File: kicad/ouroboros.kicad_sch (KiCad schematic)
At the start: 121 parts, among them J1 Eurorack Mono Jack, J10 Conn_01x03_Male, J11 Eurorack Mono Jack, J12 Eurorack Mono Jack, J13 Eurorack Mono Jack, J14 Eurorack Mono Jack, J19 Eurorack Mono Jack, J2 Eurorack Mono Jack, J20 Eurorack Mono Jack, J21 Eurorack Mono Jack, J22 Eurorack Mono Jack, J23 Eurorack Mono Jack, J24 Eurorack Mono Jack, J25 Eurorack Mono Jack, J26 Eurorack Mono Jack, J27 Eurorack Mono Jack, J28 Conn_01x06_Male, J29 Conn_01x04_Male, J3 Eurorack Mono Jack, J30 Conn_01x04_Male, J31 Conn_01x04_Male, J32 Conn_01x06_Male, J33 Conn_01x04_Male, J34 Conn_01x08_Male, J35 Conn_01x08_Male, J36 Eurorack Power Small, J38 Conn_02x04_Odd_Even, J4 Eurorack Mono Jack, J40 Conn_01x08_Female, J41 Conn_01x08_Female, J42 Conn_01x04_Female, J43 Conn_01x06_Female, J44 Conn_01x04_Female, J45 Conn_01x04_Female, J46 Conn_01x04_Female, J47 Conn_01x06_Female, J5 Eurorack Mono Jack, J6 Eurorack Mono Jack, J7 Eurorack Mono Jack, J8 Eurorack Mono Jack, J9 Eurorack Mono Jack, U1 TL074, U8 L78L05_TO92

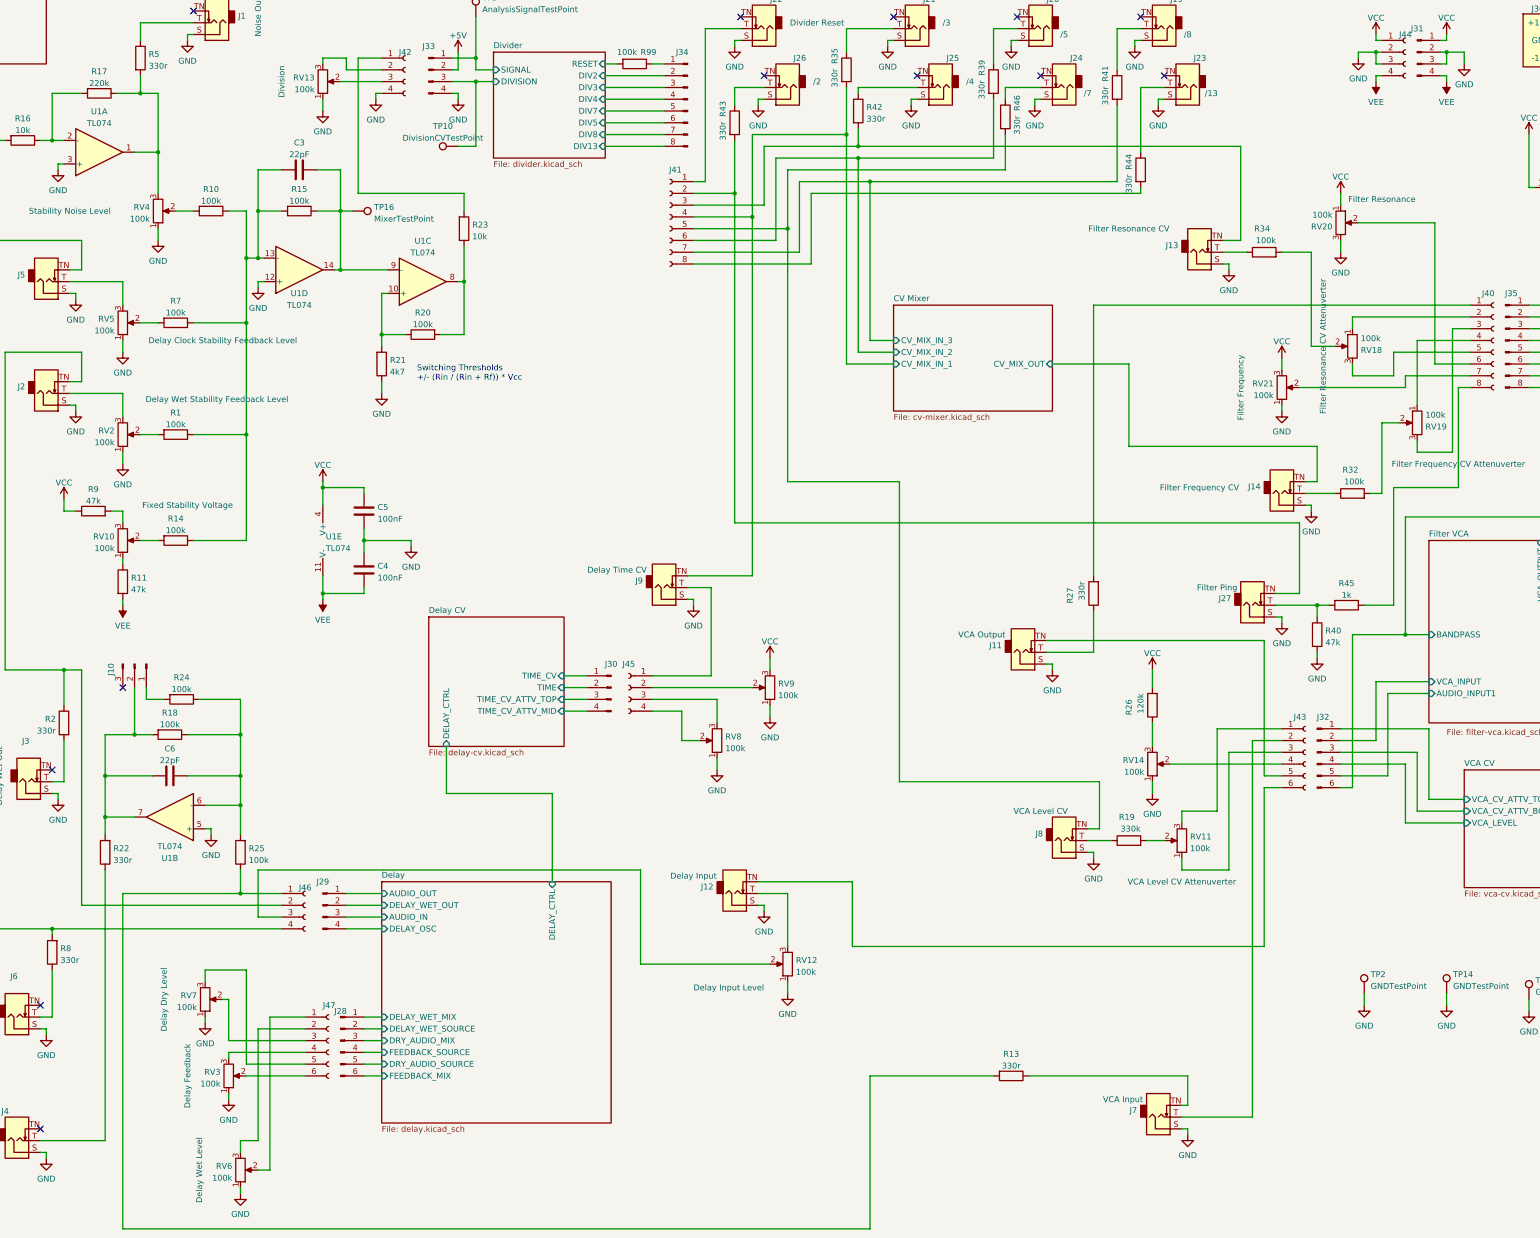
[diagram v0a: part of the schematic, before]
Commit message: Updating bom and creating part numbers list
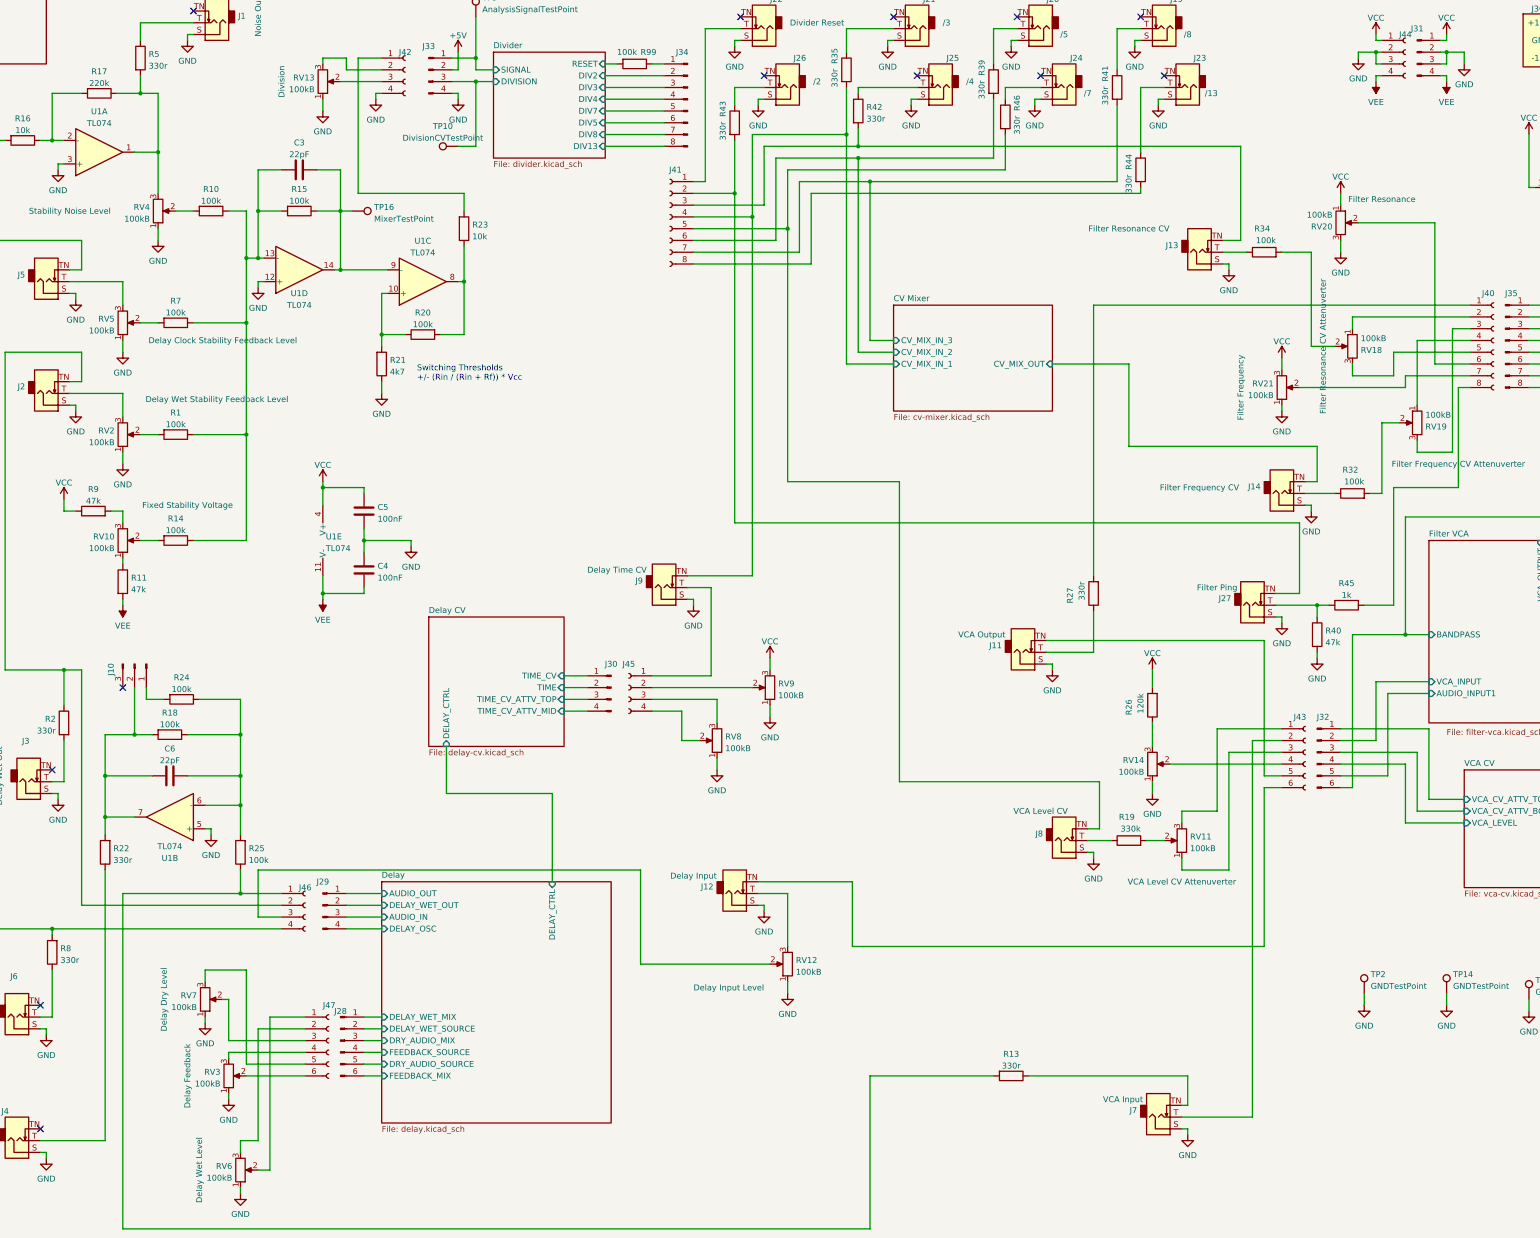
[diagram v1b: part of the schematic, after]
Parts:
- RV10, RV11, RV12, RV13, RV14, RV18, RV19, RV2, RV20, RV21, RV3, RV4, RV5, RV6, RV7, RV8, RV9: value 100k -> 100kB

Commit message: Updating for kicad 7
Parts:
- removed J36: Eurorack Power Small, eurorack-power:Eurorack_PowerHeader_2x05_P2.54mm_Shrouded, symbol Eurorack_Hardware:Eurorack Power Small
- added J36: Eurorack Power Small, Eurorack_Power:Eurorack_PowerHeader_2x05_P2.54mm_Shrouded, symbol Eurorack_Power:Eurorack Power Small
- C3, C6: footprint rumblesan-standard-parts:C_Rect_L7.0mm_W2.5mm_P5.00mm -> Rumblesan_Standard_Parts:C_Rect_L7.0mm_W2.5mm_P5.00mm; symbol rumblesan-standard-parts:C -> Rumblesan Standard Parts:C
- C4, C5: footprint rumblesan-standard-parts:C_Rect_L7.0mm_W2.5mm_P5.00mm -> Rumblesan_Standard_Parts:C_Rect_L7.0mm_W2.5mm_P5.00mm; symbol rumblesan-standard-parts:C -> Rumblesan Standard Parts:C; Spec ceramic X7R -> ceramic C0G
- C62, C63: footprint rumblesan-standard-parts:CP_Radial_D5.0mm_L11.0mm_P2.00mm_Horizontal -> Rumblesan_Standard_Parts:CP_Radial_D5.0mm_L11.0mm_P2.00mm_Horizontal; symbol rumblesan-standard-parts:C_Polarized -> Rumblesan Standard Parts:C_Polarized
- D20, D21, D7: footprint rumblesan-standard-parts:D_DO-41_SOD81_P10.16mm_Horizontal -> Rumblesan_Standard_Parts:D_DO-41_SOD81_P10.16mm_Horizontal
- H1, H2, H3, H4: footprint rumblesan-standard-parts:MountingHole_3.2mm_M3_DIN965_Pad -> Rumblesan_Standard_Parts:MountingHole_3.2mm_M3_DIN965_Pad; now left out of the parts list
- J1, J11, J12, J13, J14, J2, J20, J21, J22, J25, J26, J27, J3, J4, J5, J6, J7, J8, J9: footprint rumblesan-standard-parts:Jack_3.5mm_QingPu_WQP-PJ398SM_Vertical -> Rumblesan_Standard_Parts:Jack_3.5mm_QingPu_WQP-PJ398SM_Vertical; symbol Eurorack_Hardware:Eurorack Mono Jack -> Audio_Connectors:Eurorack_Mono_Jack
- J10: symbol Connector:Conn_01x03_Male -> Connector:Conn_01x03_Pin
- J19: footprint rumblesan-standard-parts:Jack_3.5mm_QingPu_WQP-PJ398SM_Vertical -> Rumblesan_Standard_Parts:Jack_3.5mm_QingPu_WQP-PJ398SM_Vertical; symbol Eurorack_Hardware:Eurorack Mono Jack -> Audio_Connectors:Eurorack_Mono_Jack; Name /8 -> /7
- J23: footprint rumblesan-standard-parts:Jack_3.5mm_QingPu_WQP-PJ398SM_Vertical -> Rumblesan_Standard_Parts:Jack_3.5mm_QingPu_WQP-PJ398SM_Vertical; symbol Eurorack_Hardware:Eurorack Mono Jack -> Audio_Connectors:Eurorack_Mono_Jack; Name /13 -> /8
- J24: footprint rumblesan-standard-parts:Jack_3.5mm_QingPu_WQP-PJ398SM_Vertical -> Rumblesan_Standard_Parts:Jack_3.5mm_QingPu_WQP-PJ398SM_Vertical; symbol Eurorack_Hardware:Eurorack Mono Jack -> Audio_Connectors:Eurorack_Mono_Jack; Name /7 -> /6
- J28, J32: symbol Connector:Conn_01x06_Male -> Connector:Conn_01x06_Pin
- J29, J30, J31, J33: symbol Connector:Conn_01x04_Male -> Connector:Conn_01x04_Pin
- J34, J35: symbol Connector:Conn_01x08_Male -> Connector:Conn_01x08_Pin
- J40, J41: symbol Connector:Conn_01x08_Female -> Connector:Conn_01x08_Socket
- J42, J44, J45, J46: symbol Connector:Conn_01x04_Female -> Connector:Conn_01x04_Socket
- J43, J47: symbol Connector:Conn_01x06_Female -> Connector:Conn_01x06_Socket
- R1, R10, R11, R13, R14, R15, R16, R17, R18, R19, R2, R20, R21, R22, R23, R24, R25, R26, R27, R32, R34, R35, R40, R42, R43, R45, R46, R7, R8, R9, R99: footprint rumblesan-standard-parts:R_Axial_DIN0207_L6.3mm_D2.5mm_P10.16mm_Horizontal -> Rumblesan_Standard_Parts:R_Axial_DIN0207_L6.3mm_D2.5mm_P10.16mm_Horizontal; symbol rumblesan-standard-parts:R -> Rumblesan Standard Parts:R
- R39, R41, R44, R5: footprint rumblesan-standard-parts:R_Axial_DIN0207_L6.3mm_D2.5mm_P2.54mm_Vertical -> Rumblesan_Standard_Parts:R_Axial_DIN0207_L6.3mm_D2.5mm_P2.54mm_Vertical; symbol rumblesan-standard-parts:R -> Rumblesan Standard Parts:R
- RV10, RV11, RV12, RV13, RV14, RV18, RV19, RV2, RV20, RV21, RV3, RV4, RV5, RV6, RV7, RV8, RV9: footprint rumblesan-standard-parts:Potentiometer_Alpha_RD901F-40-00D_Single_Vertical -> Rumblesan_Standard_Parts:Potentiometer_Alpha_RD901F-40-00D_Single_Vertical; symbol Device:R_Potentiometer -> Rumblesan Standard Parts:R_Potentiometer
- TP1, TP10, TP11, TP13, TP14, TP16, TP2, TP3, TP4, TP5, TP6, TP7, TP9: footprint rumblesan-standard-parts:TestPoint_Loop_D2.50mm_Drill1.0mm_LowProfile -> Rumblesan_Standard_Parts:TestPoint_Loop_D2.50mm_Drill1.0mm_LowProfile
- U1: footprint rumblesan-standard-parts:DIP-14_W7.62mm_Socket -> Rumblesan_Standard_Parts:DIP-14_W7.62mm_Socket
- U8: footprint rumblesan-standard-parts:TO-92_Inline_Wide -> Rumblesan_Standard_Parts:TO-92_Inline_Wide
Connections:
- net Divider/DIV13 is gone; now on net Divider/DIV8: J34.8 (Pin_8)
- net CV Mixer/CV_MIX_IN_1: now also J9.3 (Tip_normalize); no longer J9.TN (Tip_normalize)
- net CV Mixer/CV_MIX_OUT: now also J14.3 (Tip_normalize); no longer J14.TN (Tip_normalize)
- net Divider/DIV3: now also J34.4 (Pin_4); no longer J34.3 (Pin_3)
- net Divider/DIV4: now also J34.3 (Pin_3); no longer J34.4 (Pin_4)
- net Divider/DIV7: now also J34.7 (Pin_7); no longer J34.5 (Pin_5)
- net Divider/DIV8: no longer J34.7 (Pin_7)
- net GND: now also J1.1 (Sleeve), J11.1 (Sleeve), J12.1 (Sleeve), J13.1 (Sleeve), J14.1 (Sleeve), J19.1 (Sleeve), J2.1 (Sleeve), J20.1 (Sleeve), J21.1 (Sleeve), J22.1 (Sleeve), J23.1 (Sleeve), J24.1 (Sleeve), J25.1 (Sleeve), J26.1 (Sleeve), J27.1 (Sleeve), J3.1 (Sleeve), J4.1 (Sleeve), J5.1 (Sleeve), J6.1 (Sleeve), J7.1 (Sleeve), J8.1 (Sleeve), J9.1 (Sleeve), J36.3 (GND), J36.4 (GND), J36.5 (GND), J36.6 (GND), J36.7 (GND), J36.8 (GND); no longer J1.S (Sleeve), J11.S (Sleeve), J12.S (Sleeve), J13.S (Sleeve), J14.S (Sleeve), J19.S (Sleeve), J2.S (Sleeve), J20.S (Sleeve), J21.S (Sleeve), J22.S (Sleeve), J23.S (Sleeve), J24.S (Sleeve), J25.S (Sleeve), J26.S (Sleeve), J27.S (Sleeve), J3.S (Sleeve), J4.S (Sleeve), J5.S (Sleeve), J6.S (Sleeve), J7.S (Sleeve), J8.S (Sleeve), J9.S (Sleeve)
- net at RV12.3: now also J12.2 (Tip); no longer J12.T (Tip)
- net at R41.1: now also J19.2 (Tip); no longer J19.T (Tip)
- net at J41.1 (Pin_1): now also J22.2 (Tip); no longer J22.T (Tip)
- net at D21.1 (K): now also J36.1 (-12V), J36.2 (-12V)
- net at D20.2 (A): now also J36.10 (+12V), J36.9 (+12V)
- net at R5.1: now also J1.2 (Tip); no longer J1.T (Tip)
- net at RV2.3: now also J2.2 (Tip); no longer J2.T (Tip)
- net at R32.1: now also J14.2 (Tip); no longer J14.T (Tip)
- net at J45.1 (Pin_1): now also J9.2 (Tip); no longer J9.T (Tip)
- net at R42.1: now also J25.2 (Tip); no longer J25.T (Tip)
- net at J41.3 (Pin_3), R42.2: now also J13.3 (Tip_normalize); no longer J13.TN (Tip_normalize)
- net at R35.1: now also J21.2 (Tip); no longer J21.T (Tip)
- net at R39.1: now also J20.2 (Tip); no longer J20.T (Tip)
- net at R19.1: now also J8.2 (Tip); no longer J8.T (Tip)
- net at R13.1: now also J7.3 (Tip_normalize); no longer J7.TN (Tip_normalize)
- net at R22.1: now also J4.2 (Tip); no longer J4.T (Tip)
- net at J46.2 (Pin_2), R2.1: now also J2.3 (Tip_normalize); no longer J2.TN (Tip_normalize)
- net at J46.4 (Pin_4), R8.2: now also J5.3 (Tip_normalize); no longer J5.TN (Tip_normalize)
- net at R2.2: now also J3.2 (Tip); no longer J3.T (Tip)
- net at J43.6 (Pin_6): now also J12.3 (Tip_normalize); no longer J12.TN (Tip_normalize)
- net at R8.1: now also J6.2 (Tip); no longer J6.T (Tip)
- net at R44.1: now also J23.2 (Tip); no longer J23.T (Tip)
- net at R34.1: now also J13.2 (Tip); no longer J13.T (Tip)
- net at R40.1, R45.2: now also J27.2 (Tip); no longer J27.T (Tip)
- net at RV5.3: now also J5.2 (Tip); no longer J5.T (Tip)
- net at J41.2 (Pin_2), R43.2: now also J27.3 (Tip_normalize); no longer J27.TN (Tip_normalize)
- net at J41.5 (Pin_5), R46.2: now also J8.3 (Tip_normalize); no longer J8.TN (Tip_normalize)
- net at J43.2 (Pin_2): now also J7.2 (Tip); no longer J7.T (Tip)
- net at J43.5 (Pin_5): now also J11.3 (Tip_normalize); no longer J11.TN (Tip_normalize)
- net at R43.1: now also J26.2 (Tip); no longer J26.T (Tip)
- net at R46.1: now also J24.2 (Tip); no longer J24.T (Tip)
- net at R27.1: now also J11.2 (Tip); no longer J11.T (Tip)
- new net Divider/DIV6: J34.5 (Pin_5)
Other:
- sheet Divider ports: added DIV6; removed DIV13
- moved on the sheet: TP14, TP2, TP3

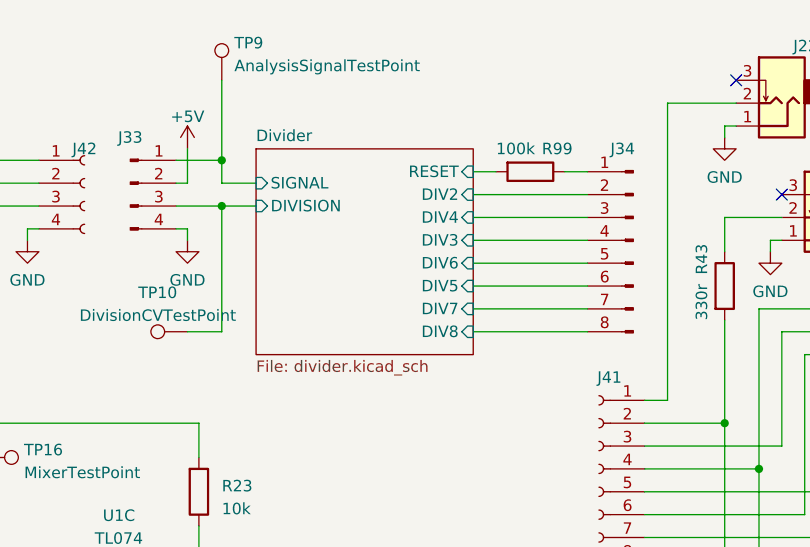
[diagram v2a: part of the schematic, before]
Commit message: Fixing issues in the divider circuitry
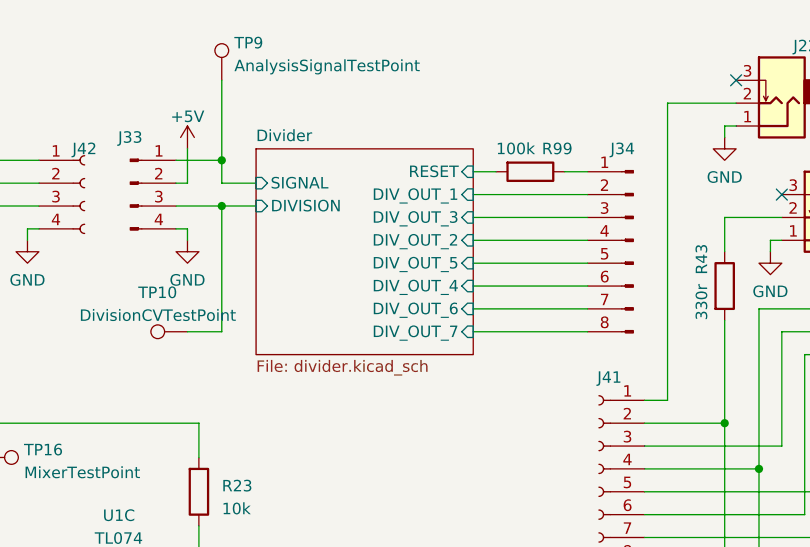
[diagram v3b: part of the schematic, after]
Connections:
- net Divider/DIV2 renamed Divider/DIV_OUT_1
- net Divider/DIV3 renamed Divider/DIV_OUT_2
- net Divider/DIV4 renamed Divider/DIV_OUT_3
- net Divider/DIV5 renamed Divider/DIV_OUT_4
- net Divider/DIV6 renamed Divider/DIV_OUT_5
- net Divider/DIV7 renamed Divider/DIV_OUT_6
- net Divider/DIV8 renamed Divider/DIV_OUT_7
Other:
- sheet Divider ports: added DIV_OUT_1, DIV_OUT_2, DIV_OUT_3, DIV_OUT_4, DIV_OUT_5, DIV_OUT_6, DIV_OUT_7; removed DIV2, DIV3, DIV4, DIV5, DIV6, DIV7, DIV8
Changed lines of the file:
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@@
       (effects (font (size 1.27 1.27)) (justify right))
     )
-    (pin "DIV8" input (at 148.59 48.26 0)
+    (pin "DIV_OUT_7" input (at 148.59 48.26 0)
       (effects (font (size 1.27 1.27)) (justify right))
     )
-    (pin "DIV7" input (at 148.59 45.72 0)
+    (pin "DIV_OUT_6" input (at 148.59 45.72 0)
       (effects (font (size 1.27 1.27)) (justify right))
     )
-    (pin "DIV4" input (at 148.59 35.56 0)
+    (pin "DIV_OUT_3" input (at 148.59 35.56 0)
       (effects (font (size 1.27 1.27)) (justify right))
     )
-    (pin "DIV5" input (at 148.59 43.18 0)
+    (pin "DIV_OUT_4" input (at 148.59 43.18 0)
       (effects (font (size 1.27 1.27)) (justify right))
     )
-    (pin "DIV3" input (at 148.59 38.1 0)
+    (pin "DIV_OUT_2" input (at 148.59 38.1 0)
       (effects (font (size 1.27 1.27)) (justify right))
     )
-    (pin "DIV2" input (at 148.59 33.02 0)
+    (pin "DIV_OUT_1" input (at 148.59 33.02 0)
       (effects (font (size 1.27 1.27)) (justify right))
     )
-    (pin "DIV6" input (at 148.59 40.64 0)
+    (pin "DIV_OUT_5" input (at 148.59 40.64 0)
       (effects (font (size 1.27 1.27)) (justify right))
     )

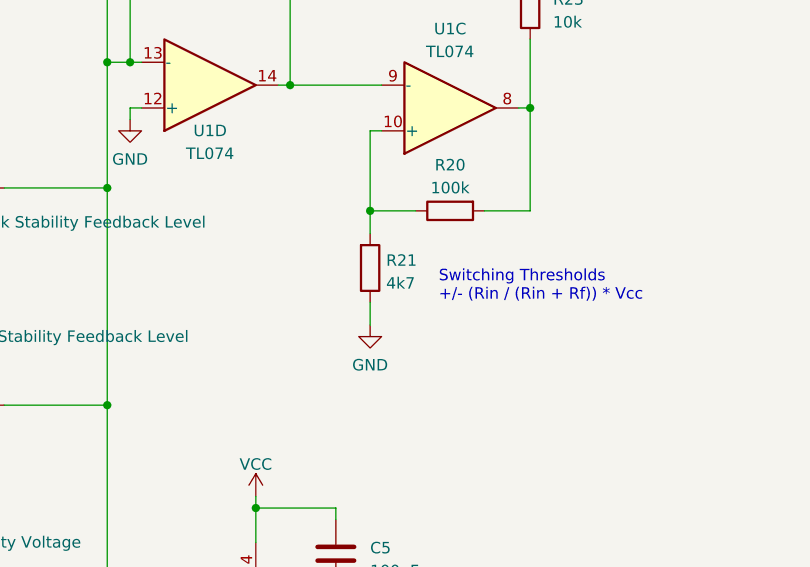
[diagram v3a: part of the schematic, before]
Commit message: Minor tweaks to rev2 values
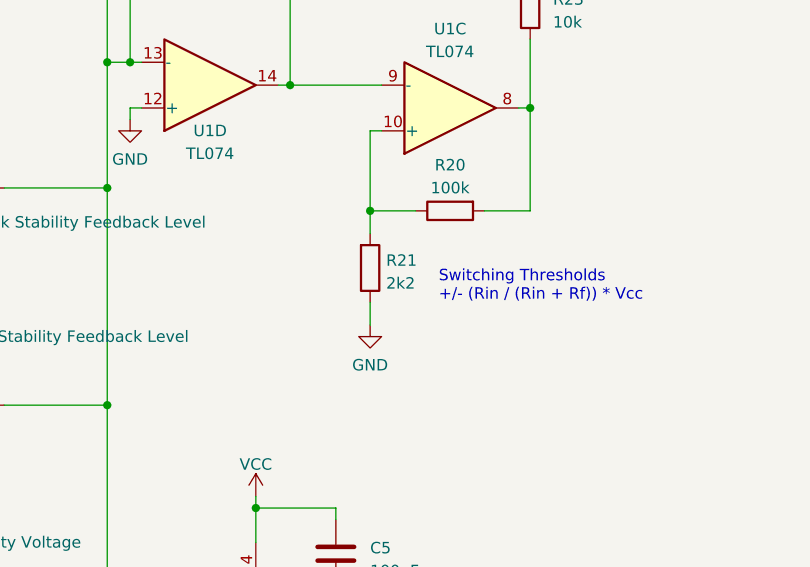
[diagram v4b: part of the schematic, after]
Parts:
- R21: value 4k7 -> 2k2
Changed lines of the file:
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@@
       (effects (font (size 1.27 1.27)) (justify right))
     )
-    (property "Value" "4k7" (at 102.108 96.9522 0)
+    (property "Value" "2k2" (at 102.108 96.9522 0)
       (effects (font (size 1.27 1.27)) (justify right))
     )
